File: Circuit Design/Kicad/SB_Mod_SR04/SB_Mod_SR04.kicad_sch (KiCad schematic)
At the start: 24 parts, among them J1 TPs, J2 GND, J3 RESET, U1 ATTINY84A

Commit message: Update before creating dev branch
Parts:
- D3: footprint Diode_SMD:D_SOD-323F -> Diode_SMD:D_SOD-123
- R9: value 1k -> 1K
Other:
- moved on the sheet: C1
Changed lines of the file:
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@@
 	)
 	(junction
-		(at 97.79 58.42)
-		(diameter 0)
-		(color 0 0 0 0)
-	)
-	(junction
 		(at 235.585 51.435)
 		(diameter 0)
@@
 	)
 	(junction
+		(at 97.79 60.325)
+		(diameter 0)
+		(color 0 0 0 0)
+	)
+	(junction
 		(at 123.19 89.535)
 		(diameter 0)
@@
 	(wire
 		(pts
-			(xy 75.565 58.42) (xy 75.565 55.245)
+			(xy 75.565 60.325) (xy 75.565 55.245)
 		)
 		(stroke
@@
 	(wire
 		(pts
-			(xy 97.79 53.34) (xy 97.79 58.42)
-		)
-		(stroke
-			(width 0)
-			(type default)
-		)
-	)
-	(wire
-		(pts
 			(xy 115.57 141.605) (xy 123.19 141.605)
 		)
@@
 	(wire
 		(pts
+			(xy 97.79 60.325) (xy 97.79 62.23)
+		)
+		(stroke
+			(width 0)
+			(type default)
+		)
+	)
+	(wire
+		(pts
 			(xy 123.19 89.535) (xy 147.32 89.535)
 		)
@@
 	(wire
 		(pts
-			(xy 80.01 58.42) (xy 75.565 58.42)
+			(xy 80.01 60.325) (xy 75.565 60.325)
+		)
+		(stroke
+			(width 0)
+			(type default)
+		)
+	)
+	(wire
+		(pts
+			(xy 97.79 53.34) (xy 97.79 60.325)
 		)
 		(stroke
@@
 	(wire
 		(pts
-			(xy 87.63 58.42) (xy 97.79 58.42)
+			(xy 87.63 60.325) (xy 97.79 60.325)
 		)
 		(stroke
@@
 	(wire
 		(pts
-			(xy 97.79 58.42) (xy 97.79 60.325)
-		)
-		(stroke
-			(width 0)
-			(type default)
-		)
-	)
-	(wire
-		(pts
 			(xy 181.61 81.28) (xy 181.61 84.455)
 		)
@@
 	)
 	(label "ECHO_H"
-		(at 95.25 69.85 0)
+		(at 95.25 71.12 0)
 		(effects
 			(font
@@
 			)
 		)
-		(property "Value" "1k"
+		(property "Value" "1K"
 			(at 95.25 76.2 90)
 			(effects
@@
 		(dnp no)
 		(property "Reference" "R8"
-			(at 180.34 73.66 90)
+			(at 180.34 73.66 0)
 			(effects
 				(font
@@
 			)
 		)
-		(property "Footprint" "Diode_SMD:D_SOD-323F"
+		(property "Footprint" "Diode_SMD:D_SOD-123"
 			(at 180.975 92.075 0)
 			(effects
@@
 	(symbol
 		(lib_id "Device:C")
-		(at 83.82 58.42 90)
+		(at 83.82 60.325 90)
 		(unit 1)
 		(exclude_from_sim no)
@@
 		(dnp no)
 		(property "Reference" "C1"
-			(at 83.82 64.135 90)
+			(at 83.82 66.04 90)
 			(effects
 				(font
@@
 		)
 		(property "Value" "0.1µ"
-			(at 83.82 62.23 90)
+			(at 83.82 64.135 90)
 			(effects
 				(font
@@
 		)
 		(property "Footprint" "Capacitor_SMD:C_1206_3216Metric_Pad1.33x1.80mm_HandSolder"
-			(at 87.63 57.4548 0)
+			(at 87.63 59.3598 0)
 			(effects
 				(font
@@
 		)
 		(property "Datasheet" "~"
-			(at 83.82 58.42 0)
+			(at 83.82 60.325 0)
 			(effects
 				(font
@@
 		)
 		(property "Description" "Unpolarized capacitor"
-			(at 83.82 58.42 0)
+			(at 83.82 60.325 0)
 			(effects
 				(font
@@
 	(symbol
 		(lib_id "power:GND")
-		(at 97.79 60.325 0)
+		(at 97.79 62.23 0)
 		(unit 1)
 		(exclude_from_sim no)
@@
 		(fields_autoplaced yes)
 		(property "Reference" "#PWR06"
-			(at 97.79 66.675 0)
+			(at 97.79 68.58 0)
 			(effects
 				(font
@@
 		)
 		(property "Value" "GND"
-			(at 97.79 64.4581 0)
+			(at 97.79 66.3631 0)
 			(effects
 				(font
@@
 		)
 		(property "Footprint" ""
-			(at 97.79 60.325 0)
+			(at 97.79 62.23 0)
 			(effects
 				(font
@@
 		)
 		(property "Datasheet" ""
-			(at 97.79 60.325 0)
+			(at 97.79 62.23 0)
 			(effects
 				(font
@@
 		)
 		(property "Description" "Power symbol creates a global label with name \"GND\" , ground"
-			(at 97.79 60.325 0)
+			(at 97.79 62.23 0)
 			(effects
 				(font

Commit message: Tidy up
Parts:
- removed D3: SD103C, Diode_SMD:D_SOD-123, symbol Device:D_Schottky_Filled
- removed SB1: LP_Sensor_Bus_IDC_8, MS_Connectors:SensorBus_2x04_P2.54mm_Vertical, symbol MS_Conn:LP_Sensor_Bus_IDC_8
- added CONN2: SENSOR_BUS, MS_Connectors:LP_Sensor_Bus_HE10_2x3, symbol MS_Conn:LP_Sensor_Bus_IDC_6
- C1, C2, C4, C5: Type (none) -> SMD
- R8: value 22K -> 10K
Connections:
- net ~{SB_INT} is gone; now on net GND: J1.4 (Pin_4)
- net +5V: now also CONN2.2 (+5V), CONN2.5 (+5V)
- net GND: now also J1.1 (Pin_1), CONN2.1 (GND), CONN2.6 (GND)
- net SB_CLK: now also J1.3 (Pin_3), CONN2.3 (CLK); no longer J1.2 (Pin_2)
- net SB_DAT: now also J1.2 (Pin_2), CONN2.4 (DAT); no longer J1.1 (Pin_1)
- net ~{SB_ACT}: no longer names the net of U1.11 (PA2)
- net ~{SB_ACT}: no longer J1.3 (Pin_3)
- net ~{SB_INT}P: no longer names the net of U1.10 (PA3)
- no-connect marks 0 -> 2
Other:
- note removed: "~{INT} should be pulled high by the hub"
- moved on the sheet: J1

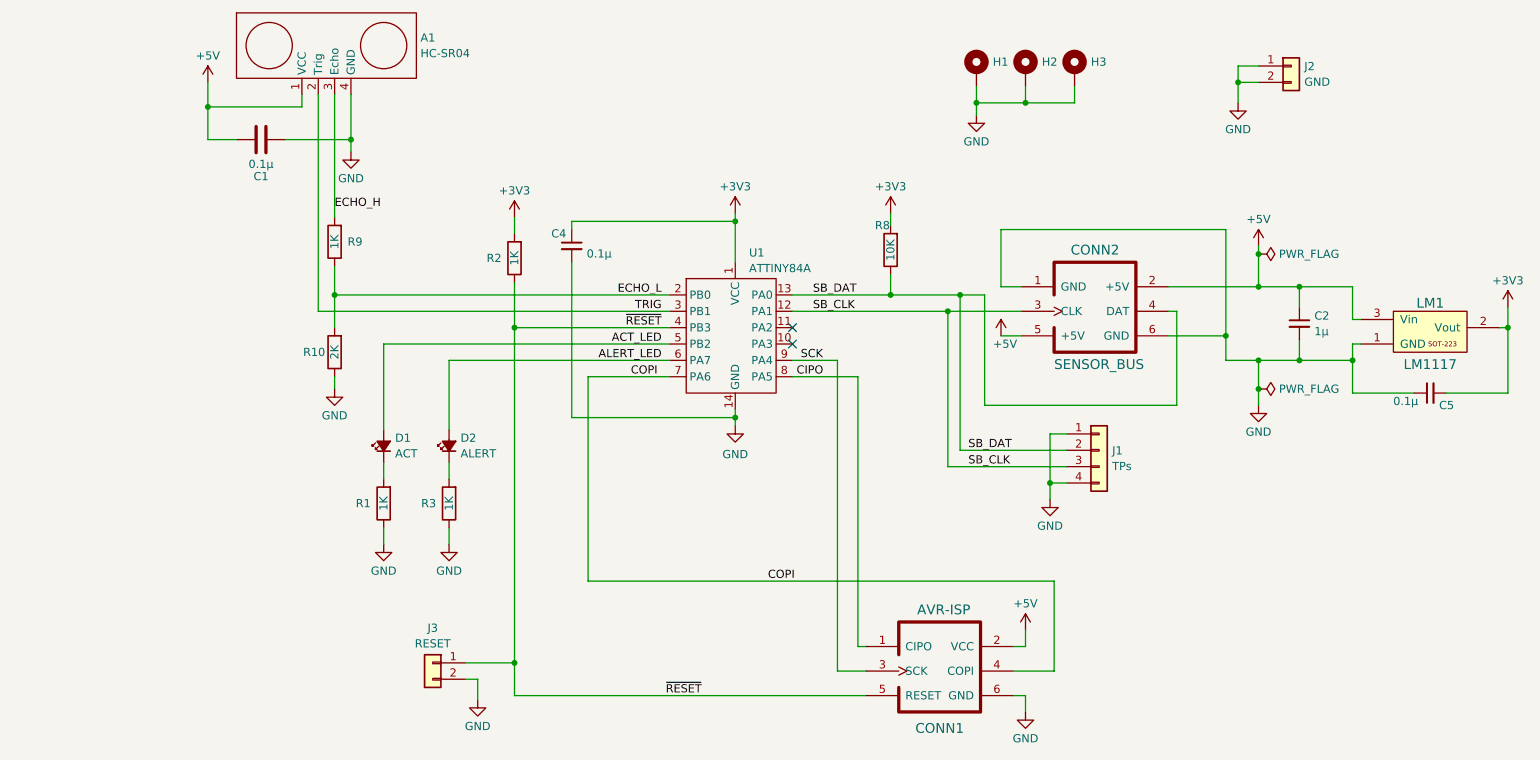
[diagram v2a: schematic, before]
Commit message: Class-based version of SR04 code. Pausing that here for now.
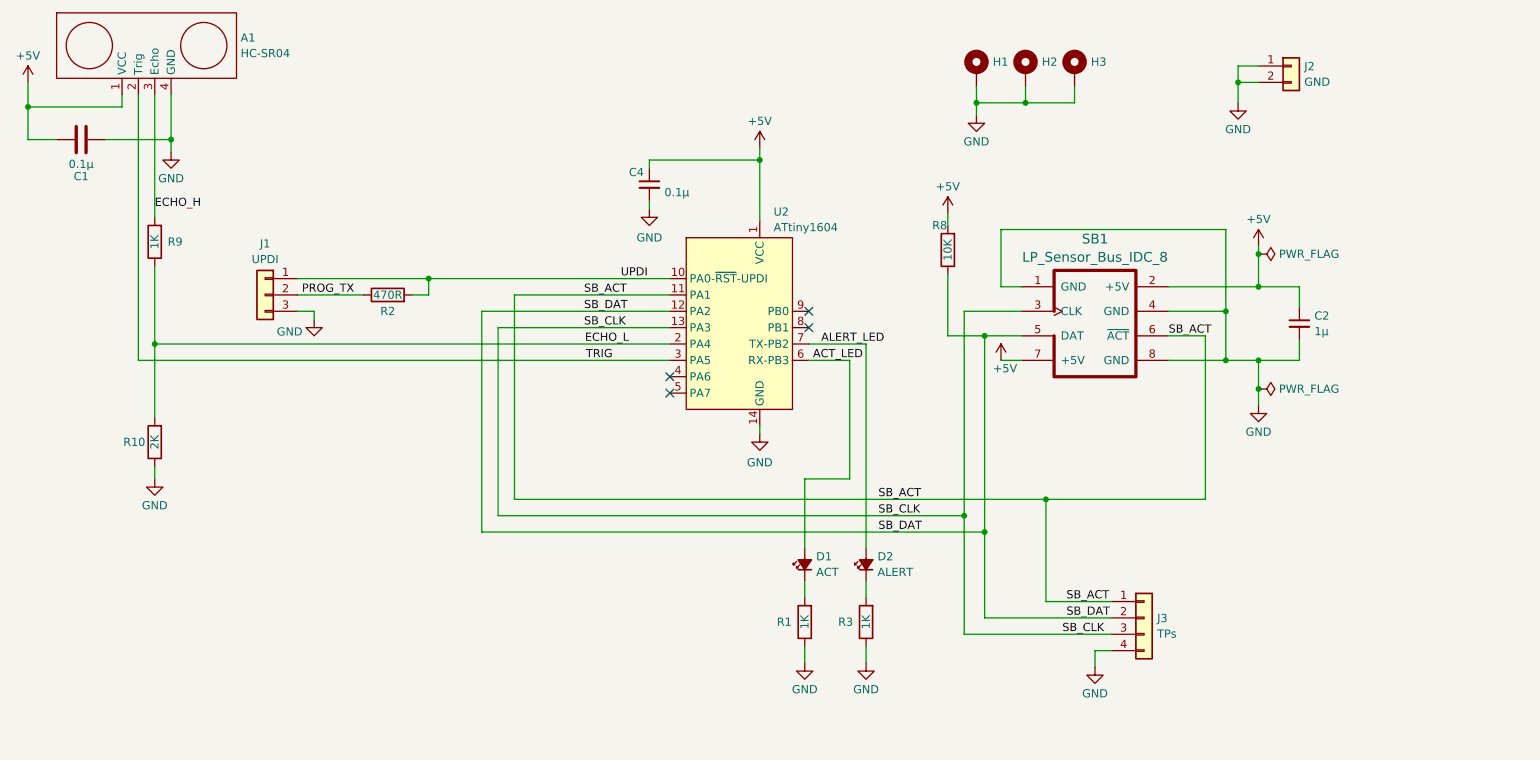
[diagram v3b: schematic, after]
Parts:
- removed C5: 0.1µ, Capacitor_SMD:C_1206_3216Metric_Pad1.33x1.80mm_HandSolder, symbol Device:C_Small
- removed CONN1: AVR-ISP, MS_Connectors:AVR_ISP_HE10_2x3, symbol MS_Conn:AVR-ISP
- removed CONN2: SENSOR_BUS, MS_Connectors:LP_Sensor_Bus_HE10_2x3, symbol MS_Conn:LP_Sensor_Bus_IDC_6
- removed J1: TPs, Connector_PinHeader_2.54mm:PinHeader_1x04_P2.54mm_Vertical, symbol Connector_Generic:Conn_01x04
- removed J3: RESET, Connector_PinHeader_2.54mm:PinHeader_1x02_P2.54mm_Vertical, symbol Connector_Generic:Conn_01x02
- removed LM1: LM1117, Package_TO_SOT_SMD:SOT-223-3_TabPin2, symbol MS_Power:LM1117
- removed U1: ATTINY84A, Package_SO:SOIC-14_3.9x8.7mm_P1.27mm, symbol MS_Microcontrollers:ATTINY84A
- added J1: UPDI, Connector_PinHeader_2.54mm:PinHeader_1x03_P2.54mm_Vertical, symbol Connector_Generic:Conn_01x03
- added J3: TPs, Connector_PinHeader_2.54mm:PinHeader_1x04_P2.54mm_Vertical, symbol Connector_Generic:Conn_01x04
- added SB1: LP_Sensor_Bus_IDC_8, MS_Connectors:SensorBus_2x04_P2.54mm_Vertical, symbol MS_Conn:LP_Sensor_Bus_IDC_8
- added U2: ATtiny1604, Package_SO:SOIC-14_3.9x8.7mm_P1.27mm, symbol MS_Microcontrollers:ATtiny1604-SS
- R2: value 1K -> 470R
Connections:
- net +5V: now also C4.1, R8.2, SB1.2 (+5V), SB1.7 (+5V), U2.1 (VCC)
- net ACT_LED: now also U2.6 (RX-PB3)
- net ALERT_LED: now also U2.7 (TX-PB2)
- net ECHO_L: now also U2.2 (PA4)
- net GND: now also J1.3 (Pin_3), J3.4 (Pin_4), SB1.1 (GND), SB1.4 (GND), SB1.8 (GND), U2.14 (GND)
- net SB_CLK: now also J3.3 (Pin_3), SB1.3 (CLK), U2.13 (PA3)
- net SB_DAT: now also J3.2 (Pin_2), SB1.5 (DAT), U2.12 (PA2)
- net TRIG: now also U2.3 (PA5)
- removed net +3V3: C4.1, R2.2, R8.2
- net ~{RESET} renamed PROG_TX
- net PROG_TX: now also J1.2 (Pin_2)
- new net SB_ACT: J3.1 (Pin_1), SB1.6 (~{ACT}), U2.11 (PA1)
- new net UPDI: J1.1 (Pin_1), R2.2, U2.10 (PA0-~{RST}-UPDI)
- no-connect marks 2 -> 4
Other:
- moved on the sheet: A1, C1, C4, D1, D2, R1, R10, R3, R8, R9

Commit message: Reorganised
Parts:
- removed R10: 2K, MS_Favourites:Resistor_SMD_1206_HandSolder, symbol Device:R
- removed R9: 1K, MS_Favourites:Resistor_SMD_1206_HandSolder, symbol Device:R
- added CONN1: AVR-UPDI-ICE, Connector_PinHeader_2.54mm:PinHeader_2x03_P2.54mm_Vertical, symbol MS_Conn:AVR-UPDI-ICE
- added D3: SD103C, Diode_SMD:D_SOD-123, symbol Device:D_Schottky_Small_Filled
- added J4: SERIAL, Connector_PinHeader_2.54mm:PinHeader_1x03_P2.54mm_Vertical, symbol Connector_Generic:Conn_01x03
- added J5: GPIO, Connector_PinHeader_2.54mm:PinHeader_1x02_P2.54mm_Vertical, symbol Connector_Generic:Conn_01x02
- R2: value 470R -> 10K
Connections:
- net ECHO_L is gone; now on net TRIG: U2.2 (PA4)
- net +5V: now also R2.2, CONN1.2 (VCC)
- net ACT_LED: now also U2.8 (PB1); no longer U2.6 (RX-PB3)
- net ALERT_LED: now also U2.9 (PB0); no longer U2.7 (TX-PB2)
- net GND: now also CONN1.6 (GND), J4.3 (Pin_3)
- net PROG_TX: now also D3.1 (K); no longer R2.1
- net TRIG: no longer U2.3 (PA5)
- net UPDI: now also R2.1, CONN1.1 (UPDI), D3.2 (A); no longer R2.2
- net A6: now reaches U2.4 (PA6)
- net A6: now also J5.1 (Pin_1)
- net A7: now reaches U2.5 (PA7)
- net A7: now also J5.2 (Pin_2)
- net ECHO_H renamed ECHO
- net ECHO: now also U2.3 (PA5)
- new net RX: J4.2 (Pin_2), U2.6 (RX-PB3)
- new net TX: J4.1 (Pin_1), U2.7 (TX-PB2)
- no-connect marks 4 -> 0
